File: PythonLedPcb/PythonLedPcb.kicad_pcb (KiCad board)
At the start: 2 copper layers, 53 x 12 mm, 8 parts

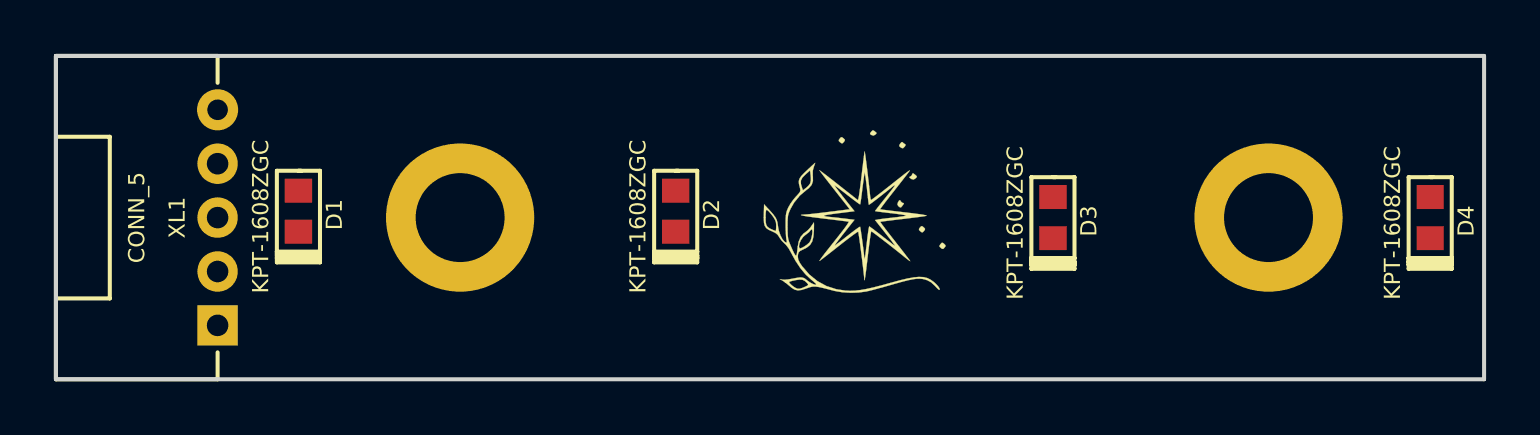
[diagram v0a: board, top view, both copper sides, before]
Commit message: V3 sent to factory
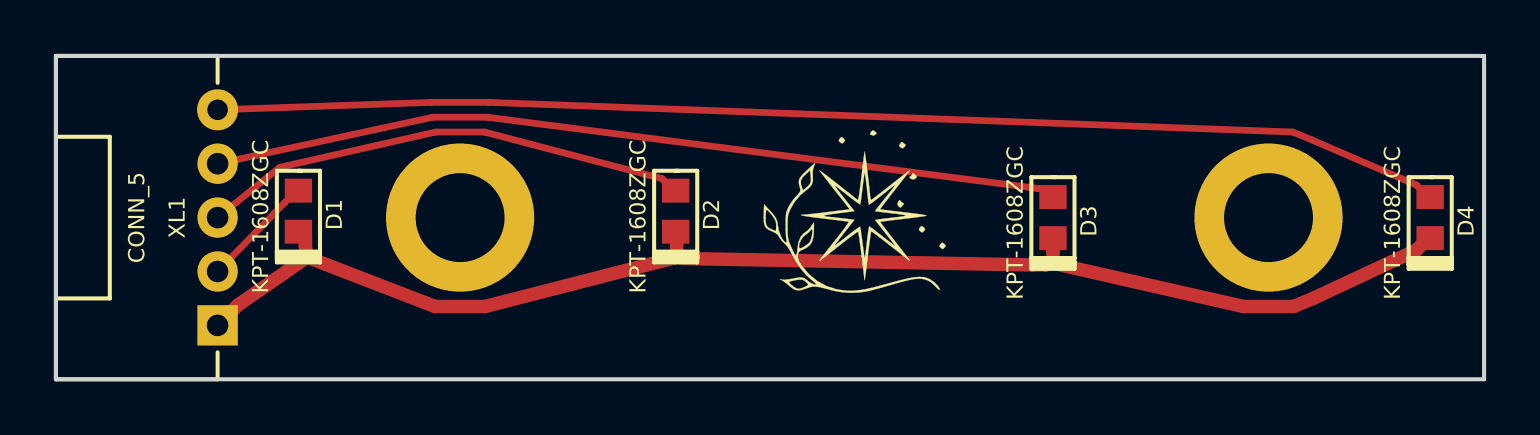
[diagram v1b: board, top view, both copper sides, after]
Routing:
- net Net-(D1-PadC): track 0.00 -> 50.2 mm
- net Net-(D4-PadA): track 0.00 -> 45.6 mm
- net Net-(D3-PadA): track 0.00 -> 31.5 mm
- net Net-(D2-PadA): track 0.00 -> 18.2 mm
- net Net-(D1-PadA): track 0.00 -> 4.24 mm
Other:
- rule pad_to_mask_clearance: 0.2 -> 0.15
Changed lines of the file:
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@@
     (thickness 1.6)
     (drawings 14)
-    (tracks 0)
+    (tracks 52)
     (zones 0)
     (modules 8)
@@
     (pad_size 1.524 1.524)
     (pad_drill 0.762)
-    (pad_to_mask_clearance 0.2)
+    (pad_to_mask_clearance 0.15)
     (aux_axis_origin 0 0)
-    (visible_elements FFFFF77F)
+    (visible_elements 7FFFFF7F)
     (pcbplotparams
-      (layerselection 0x010fc_ffffffff)
-      (usegerberextensions false)
-      (usegerberattributes false)
+      (layerselection 0x010e0_ffffffff)
+      (usegerberextensions true)
+      (usegerberattributes true)
       (usegerberadvancedattributes false)
       (creategerberjobfile false)
@@
       (plotinvisibletext false)
       (padsonsilk false)
-      (subtractmaskfromsilk false)
+      (subtractmaskfromsilk true)
       (outputformat 1)
       (mirror false)
-      (drillshape 1)
+      (drillshape 0)
       (scaleselection 1)
-      (outputdirectory ""))
+      (outputdirectory Gerber))
   )
   (net 0 "")
@@
   (gr_line (start 188 77) (end 188 89) (layer Edge.Cuts) (width 0.15))
   (gr_line (start 135 77) (end 188 77) (layer Edge.Cuts) (width 0.15))
+  (segment (start 143.617 82.3195) (end 144 82) (width 0.25) (layer F.Cu) (net 1))
+  (segment (start 143.492 82.4445) (end 143.617 82.3195) (width 0.25) (layer F.Cu) (net 1))
+  (segment (start 141 85) (end 143.492 82.4445) (width 0.25) (layer F.Cu) (net 1))
+  (segment (start 185.742 83.9565) (end 186 83.762) (width 0.5) (layer F.Cu) (net 2))
+  (segment (start 185.492 84.2065) (end 185.742 83.9565) (width 0.5) (layer F.Cu) (net 2))
+  (segment (start 181.6775 85.9895) (end 185.492 84.2065) (width 0.5) (layer F.Cu) (net 2))
+  (segment (start 180.9277 86.3001) (end 181.6775 85.9895) (width 0.5) (layer F.Cu) (net 2))
+  (segment (start 179.0723 86.3001) (end 180.9277 86.3001) (width 0.5) (layer F.Cu) (net 2))
+  (segment (start 172.0506 84.7071) (end 179.0723 86.3001) (width 0.5) (layer F.Cu) (net 2))
+  (segment (start 172.0001 84.6566) (end 172.0506 84.7071) (width 0.5) (layer F.Cu) (net 2))
+  (segment (start 172.0001 83.9565) (end 172 83.762) (width 0.5) (layer F.Cu) (net 2))
+  (segment (start 172.0001 84.2065) (end 172.0001 83.9565) (width 0.5) (layer F.Cu) (net 2))
+  (segment (start 172.0001 84.6566) (end 172.0001 84.2065) (width 0.5) (layer F.Cu) (net 2))
+  (segment (start 171.9494 84.7072) (end 172.0001 84.6566) (width 0.5) (layer F.Cu) (net 2))
+  (segment (start 171.7199 84.7566) (end 171.9494 84.7072) (width 0.5) (layer F.Cu) (net 2))
+  (segment (start 171.2641 84.7566) (end 171.7199 84.7566) (width 0.5) (layer F.Cu) (net 2))
+  (segment (start 158.2801 84.5186) (end 171.2641 84.7566) (width 0.5) (layer F.Cu) (net 2))
+  (segment (start 158.061 84.4442) (end 158.2801 84.5186) (width 0.5) (layer F.Cu) (net 2))
+  (segment (start 158.0353 84.4186) (end 158.061 84.4442) (width 0.5) (layer F.Cu) (net 2))
+  (segment (start 158.0353 83.7185) (end 158 83.524) (width 0.5) (layer F.Cu) (net 2))
+  (segment (start 158.0353 83.9685) (end 158.0353 83.7185) (width 0.5) (layer F.Cu) (net 2))
+  (segment (start 158.0353 84.4186) (end 158.0353 83.9685) (width 0.5) (layer F.Cu) (net 2))
+  (segment (start 157.9597 84.4941) (end 158.0353 84.4186) (width 0.5) (layer F.Cu) (net 2))
+  (segment (start 150.9277 86.3001) (end 157.9597 84.4941) (width 0.5) (layer F.Cu) (net 2))
+  (segment (start 149.0723 86.3001) (end 150.9277 86.3001) (width 0.5) (layer F.Cu) (net 2))
+  (segment (start 144.3218 84.4685) (end 149.0723 86.3001) (width 0.5) (layer F.Cu) (net 2))
+  (segment (start 144.258 83.7185) (end 144 83.524) (width 0.5) (layer F.Cu) (net 2))
+  (segment (start 144.258 83.9685) (end 144.258 83.7185) (width 0.5) (layer F.Cu) (net 2))
+  (segment (start 144.258 84.0721) (end 144.258 83.9685) (width 0.5) (layer F.Cu) (net 2))
+  (segment (start 144.3218 84.4685) (end 144.258 84.0721) (width 0.5) (layer F.Cu) (net 2))
+  (segment (start 141.75 86.25) (end 144.3218 84.4685) (width 0.5) (layer F.Cu) (net 2))
+  (segment (start 141.5 86.5) (end 141.75 86.25) (width 0.5) (layer F.Cu) (net 2))
+  (segment (start 141 87) (end 141.5 86.5) (width 0.5) (layer F.Cu) (net 2))
+  (segment (start 157.617 81.6805) (end 158 82) (width 0.25) (layer F.Cu) (net 3))
+  (segment (start 157.492 81.5555) (end 157.617 81.6805) (width 0.25) (layer F.Cu) (net 3))
+  (segment (start 150.9028 79.8249) (end 157.492 81.5555) (width 0.25) (layer F.Cu) (net 3))
+  (segment (start 149.0972 79.8249) (end 150.9028 79.8249) (width 0.25) (layer F.Cu) (net 3))
+  (segment (start 143.3159 81.1304) (end 149.0972 79.8249) (width 0.25) (layer F.Cu) (net 3))
+  (segment (start 141 83) (end 143.3159 81.1304) (width 0.25) (layer F.Cu) (net 3))
+  (segment (start 171.617 81.9185) (end 172 82.238) (width 0.25) (layer F.Cu) (net 4))
+  (segment (start 171.492 81.9185) (end 171.617 81.9185) (width 0.25) (layer F.Cu) (net 4))
+  (segment (start 171.4402 81.9185) (end 171.492 81.9185) (width 0.25) (layer F.Cu) (net 4))
+  (segment (start 151.0123 79.2748) (end 171.4402 81.9185) (width 0.25) (layer F.Cu) (net 4))
+  (segment (start 148.9877 79.2748) (end 151.0123 79.2748) (width 0.25) (layer F.Cu) (net 4))
+  (segment (start 141 81) (end 148.9877 79.2748) (width 0.25) (layer F.Cu) (net 4))
+  (segment (start 185.617 81.9185) (end 186 82.238) (width 0.25) (layer F.Cu) (net 5))
+  (segment (start 185.492 81.7935) (end 185.617 81.9185) (width 0.25) (layer F.Cu) (net 5))
+  (segment (start 181.6067 80.1165) (end 185.492 81.7935) (width 0.25) (layer F.Cu) (net 5))
+  (segment (start 180.9028 79.8249) (end 181.6067 80.1165) (width 0.25) (layer F.Cu) (net 5))
+  (segment (start 151.072 78.7247) (end 180.9028 79.8249) (width 0.25) (layer F.Cu) (net 5))
+  (segment (start 148.928 78.7247) (end 151.072 78.7247) (width 0.25) (layer F.Cu) (net 5))
+  (segment (start 141 79) (end 148.928 78.7247) (width 0.25) (layer F.Cu) (net 5))
 )
